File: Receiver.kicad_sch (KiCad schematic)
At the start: 20 parts, among them J2 UFL_Antennna, Y1 52Mhz/8pF, Y2 52Mhz/8pF

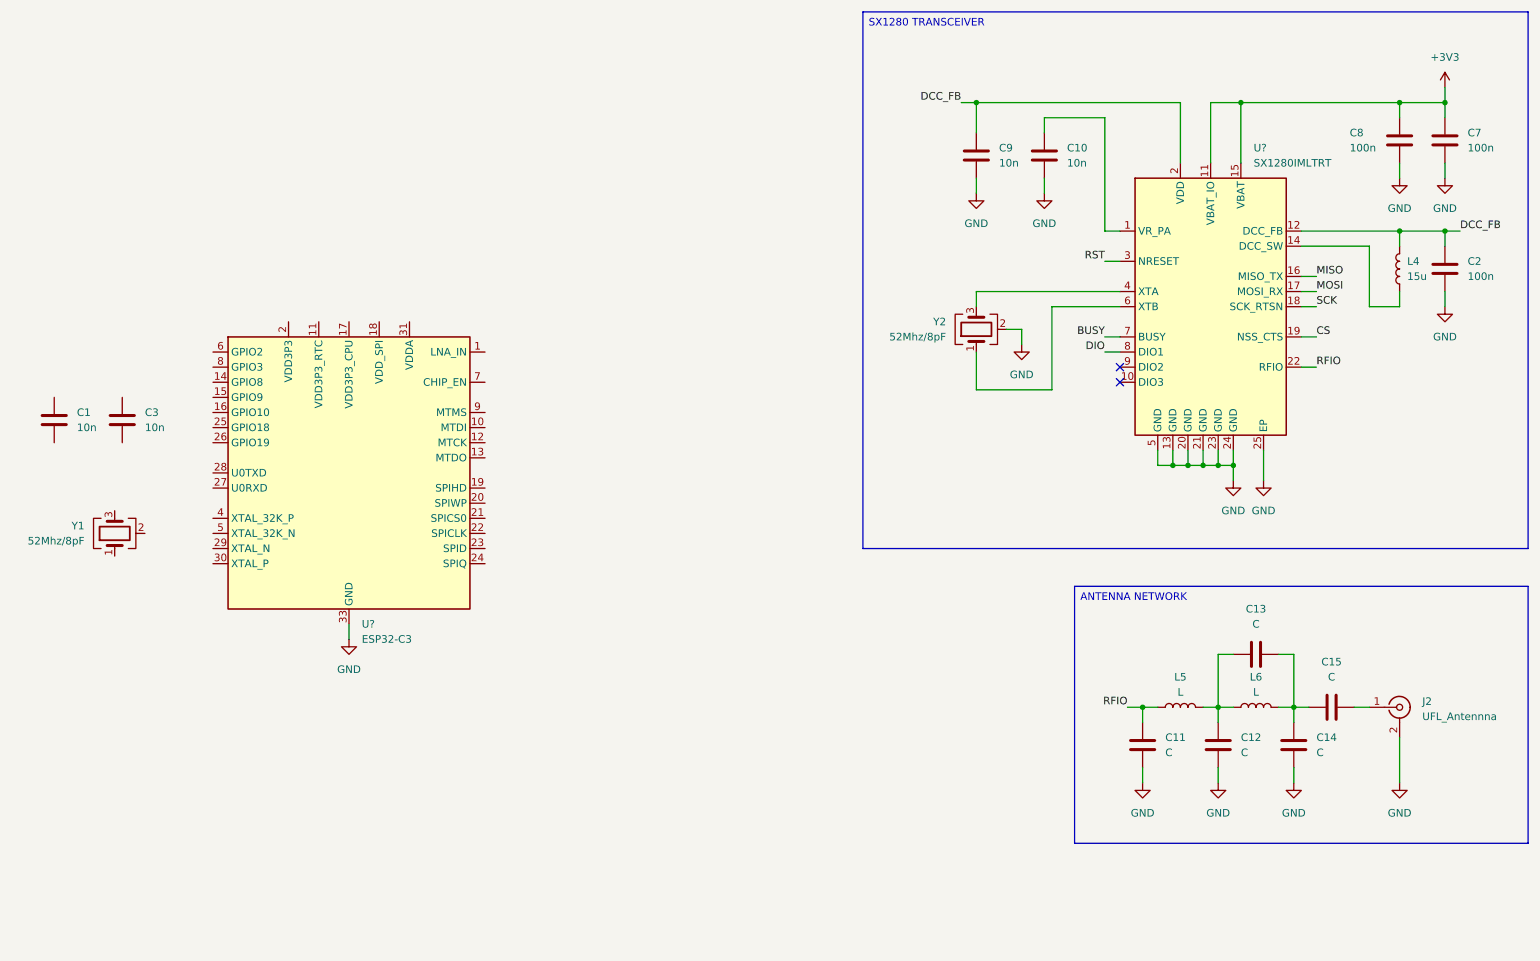
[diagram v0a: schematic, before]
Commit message: Receiver design
Updated the receiver schematic.

TODO:
Review the receiver schematic.
Implement sensor conditioning.
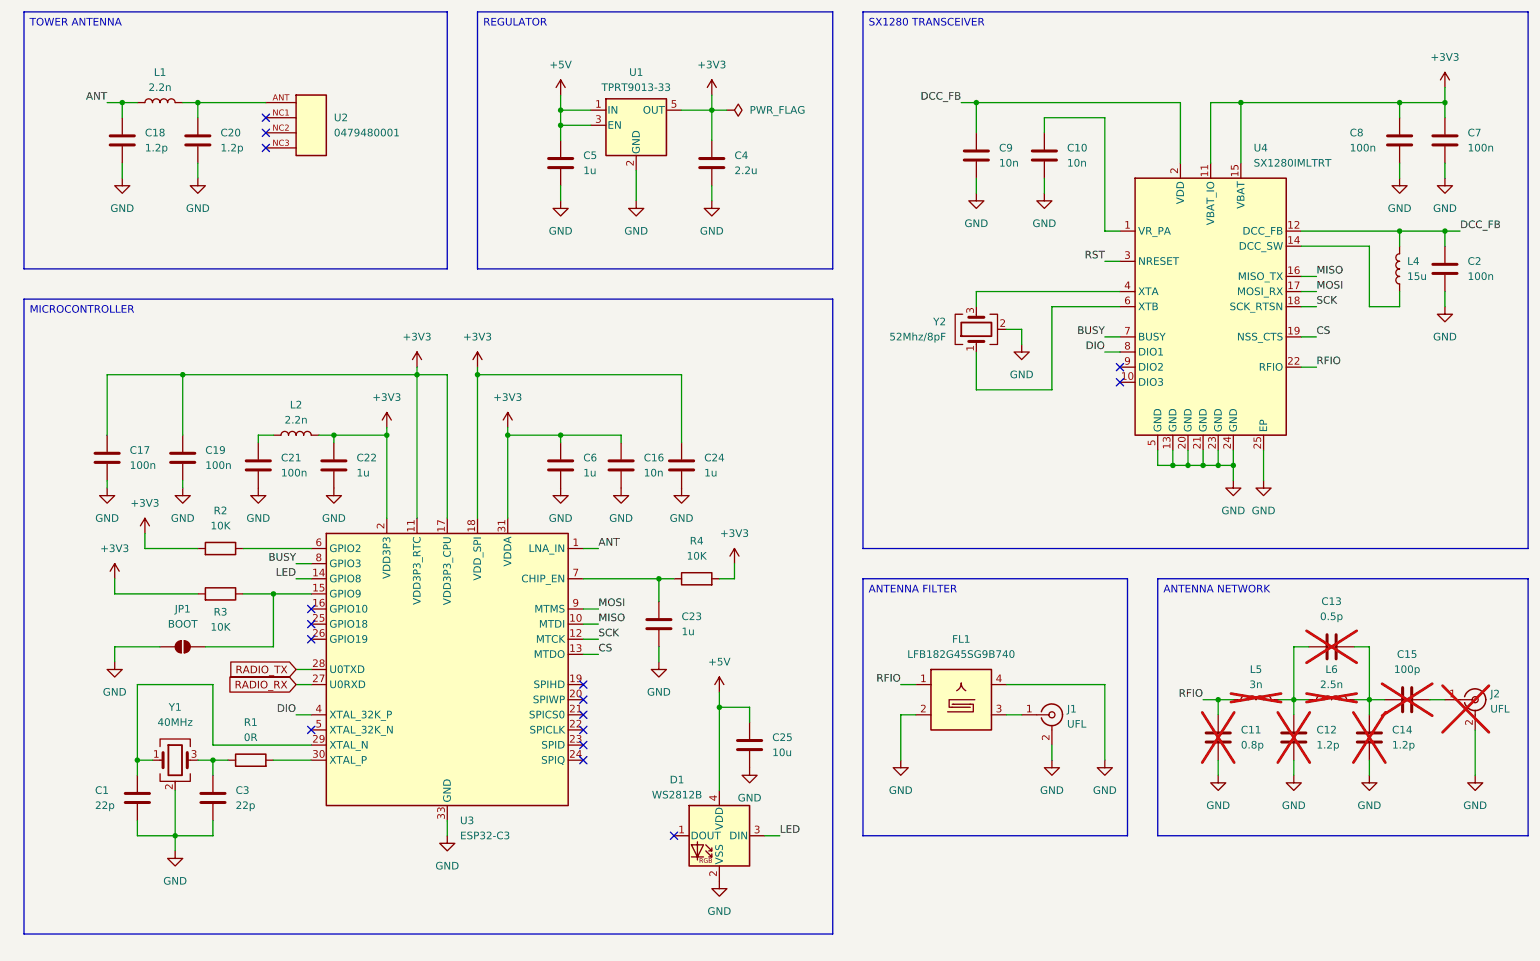
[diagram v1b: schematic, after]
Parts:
- added C16: 10n, symbol Device:C
- added C17, C19, C21: 100n, symbol Device:C
- added C18, C20: 1.2p, symbol Device:C
- added C22, C23, C24, C5, C6: 1u, symbol Device:C
- added C25: 10u, symbol Device:C
- added C4: 2.2u, symbol Device:C
- added D1: WS2812B, Custom_Parts:WS2812B-2020, symbol LED:WS2812B-2020
- added FL1: LFB182G45SG9B740, Custom_Parts:LFB182G45SG9B740, symbol Custom_Parts:LFB182G45SG9B740
- added J1: UFL, Connector_Coaxial:U.FL_Hirose_U.FL-R-SMT-1_Vertical, symbol Connector:Conn_Coaxial
- added JP1: BOOT, Jumper:SolderJumper-2_P1.3mm_Open_RoundedPad1.0x1.5mm, symbol Jumper:SolderJumper_2_Open
- added L1, L2: 2.2n, symbol Device:L
- added R1: 0R, symbol Device:R
- added R2, R3, R4: 10K, symbol Device:R
- added U1: TPRT9013-33, Package_TO_SOT_SMD:SOT-23-5, symbol Regulator_Linear:TLV70233_SOT23-5
- added U2: 0479480001, Custom_Parts:0479480001, symbol Custom_Parts:0479480001
- C1, C3: value 10n -> 22p
- C11: value C -> 0.8p; now not fitted; now left out of the parts list
- C12, C14: value C -> 1.2p; now not fitted; now left out of the parts list
- C13: value C -> 0.5p; now not fitted; now left out of the parts list
- C15: value C -> 100p; now not fitted; now left out of the parts list
- J2: value UFL_Antennna -> UFL; now not fitted; now left out of the parts list
- L5: value L -> 3n; now not fitted; now left out of the parts list
- L6: value L -> 2.5n; now not fitted; now left out of the parts list
- Y1: value 52Mhz/8pF -> 40MHz
- gave numbers to parts that had none: 2
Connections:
- net +3V3: now also U3.11 (VDD3P3_RTC), U3.17 (VDD3P3_CPU), U3.18 (VDD_SPI), U3.2 (VDD3P3), U3.3 (VDD3P3), U3.31 (VDDA), U3.32 (VDDA), C16.1, C17.1, C19.1, C22.1, C24.1, C4.1, C6.1, L2.2, R2.2, R3.2, R4.2, U1.5 (OUT)
- net BUSY: now also U3.8 (GPIO3)
- net CS: now also U3.13 (MTDO)
- net DIO: now also U3.4 (XTAL_32K_P)
- net GND: now also C1.2, C3.2, Y1.2 (G), Y1.4 (G), C16.2, C17.2, C18.2, C19.2, C20.2, C21.2, C22.2, C23.2, C24.2, C25.2, C4.2, C5.2, C6.2, D1.2 (VSS), FL1.2, FL1.4, FL1.5, J1.2 (Ext), JP1.1 (A), U1.2 (GND)
- net MISO: now also U3.10 (MTDI)
- net MOSI: now also U3.9 (MTMS)
- net RFIO: now also FL1.1
- net SCK: now also U3.12 (MTCK)
- net ANT: now reaches U3.1 (LNA_IN)
- net ANT: now also C18.1, L1.1
- net LED: now reaches U3.14 (GPIO8)
- net LED: now also D1.3 (DIN)
- net at U3.15 (GPIO9): now also JP1.2 (B), R3.1
- net RADIO_RX: now reaches U3.27 (U0RXD)
- net RADIO_TX: now reaches U3.28 (U0TXD)
- net at U3.29 (XTAL_N): now also C1.1, Y1.1
- net at U3.30 (XTAL_P): now also R1.2
- net at U3.6 (GPIO2): now also R2.1
- net at U3.7 (CHIP_EN): now also C23.1, R4.1
- net at Y1.3: now also C3.1, R1.1
- new net: C20.1, L1.2, U2.ANT
- new net: C21.1, L2.1
- new net: FL1.3, J1.1 (In)
- new net +5V: C25.1, C5.1, D1.4 (VDD), U1.1 (IN), U1.3 (EN)
- no-connect marks 2 -> 16
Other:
- moved on the sheet: C1, C3, U3, Y1

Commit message: Sensors design
Updated the inertial measurement unit schematic.
Updated the power monitor schematic.
Updated the barometer schematic.
Updated the receiver schematic.

TODO:
Review the sensors schematic.
Implement ESC schematic.
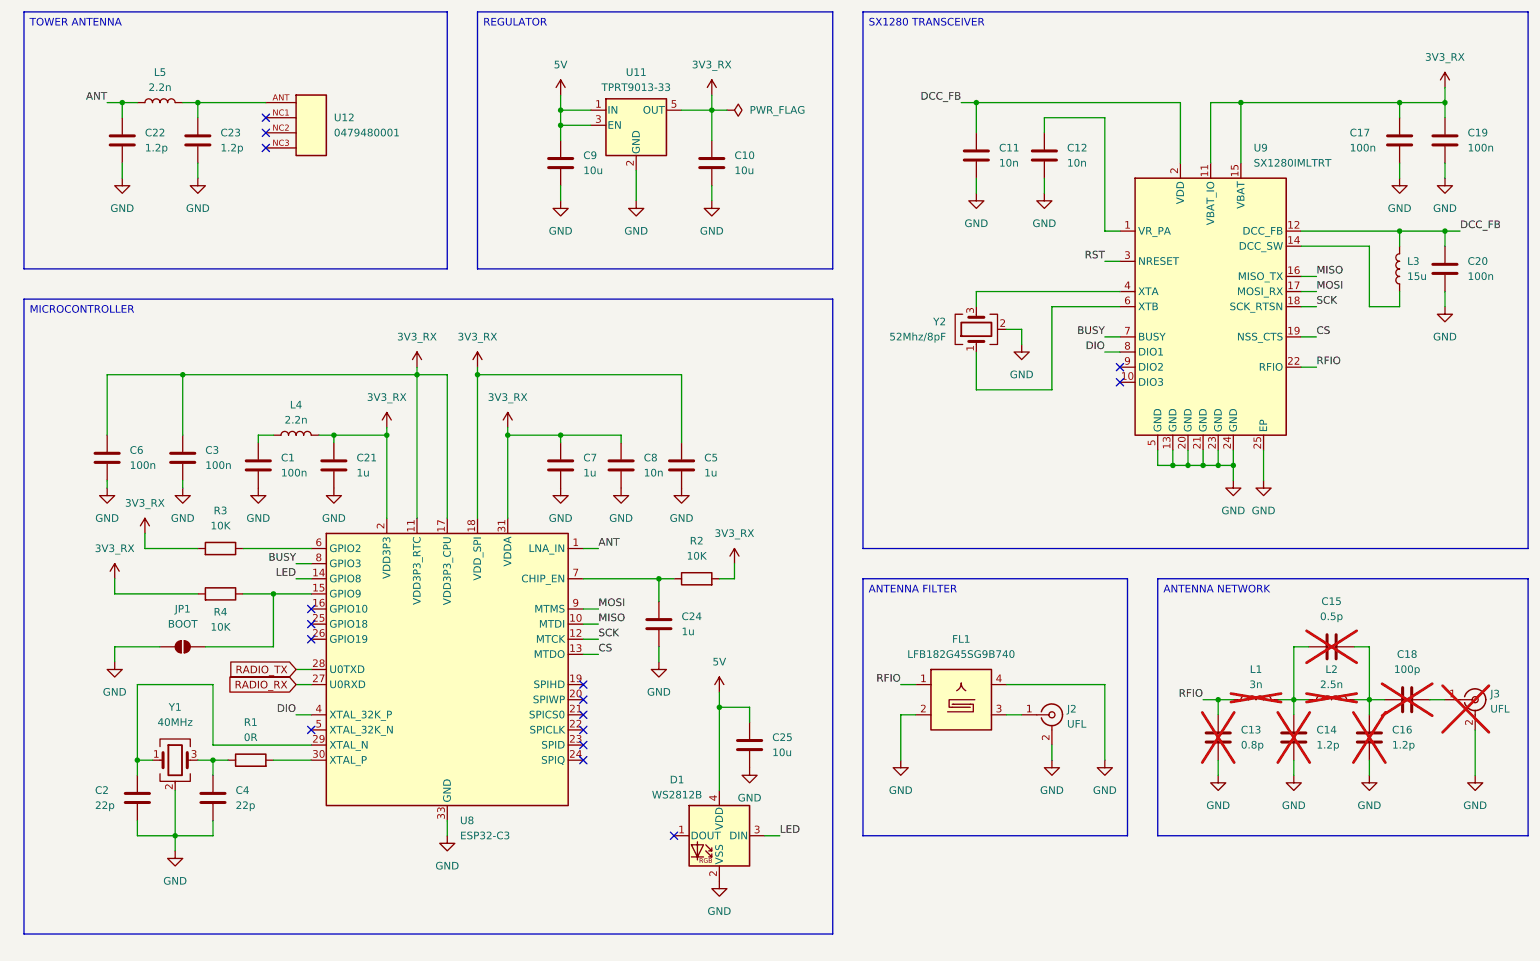
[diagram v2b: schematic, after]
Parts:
- C10: renamed from C4; value 2.2u -> 10u
- C9: renamed from C5; value 1u -> 10u
- renumbered C21 to C1, C9 to C11, C10 to C12, C11 to C13, C12 to C14, C13 to C15, C14 to C16, C8 to C17, C15 to C18, C7 to C19, C1 to C2, C2 to C20, C22 to C21, C18 to C22, C20 to C23, C23 to C24, C19 to C3, C3 to C4, C24 to C5, C17 to C6, C6 to C7, C16 to C8, J1 to J2, J2 to J3, L5 to L1, L6 to L2, L4 to L3, L2 to L4, L1 to L5, R4 to R2, R2 to R3, R3 to R4, U1 to U11, U2 to U12, U3 to U8, U4 to U9
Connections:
- net +3V3 renamed 3V3_RX
- net +5V renamed 5V

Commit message: ESC design
Updated the ESC schematic.
Replaces the INA 226 with INA230.
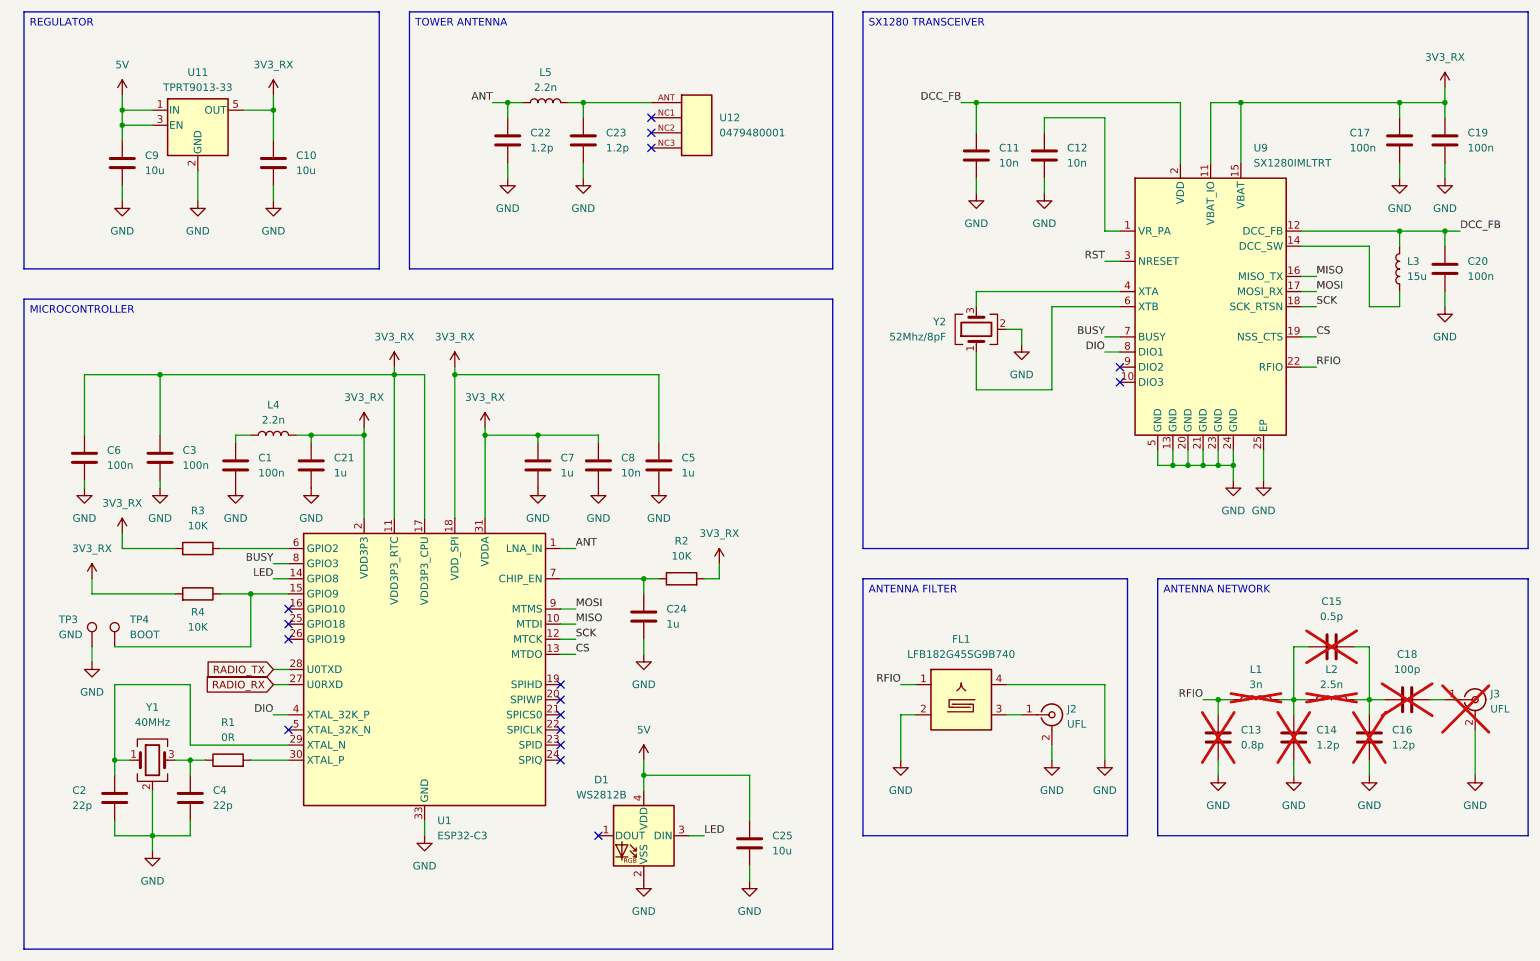
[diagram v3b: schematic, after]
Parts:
- removed JP1: BOOT, Jumper:SolderJumper-2_P1.3mm_Open_RoundedPad1.0x1.5mm, symbol Jumper:SolderJumper_2_Open
- removed U8: ESP32-C3, Package_DFN_QFN:QFN-32-1EP_5x5mm_P0.5mm_EP3.7x3.7mm, symbol MCU_Espressif:ESP32-C3
- added TP3: GND, TestPoint:TestPoint_Pad_D1.0mm, symbol Connector:TestPoint
- added TP4: BOOT, TestPoint:TestPoint_Pad_D1.0mm, symbol Connector:TestPoint
- added U1: ESP32-C3, Package_DFN_QFN:QFN-32-1EP_5x5mm_P0.5mm_EP3.7x3.7mm, symbol Custom_Parts:ESP32-C3
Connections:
- net 3V3_RX: now also U1.11 (VDD3P3_RTC), U1.17 (VDD3P3_CPU), U1.18 (VDD_SPI), U1.2 (VDD3P3), U1.3 (VDD3P3), U1.31 (VDDA), U1.32 (VDDA)
- net ANT: now also U1.1 (LNA_IN)
- net BUSY: now also U1.8 (GPIO3)
- net CS: now also U1.13 (MTDO)
- net DIO: now also U1.4 (XTAL_32K_P)
- net GND: now also TP3.1, U1.33 (GND)
- net LED: now also U1.14 (GPIO8)
- net MISO: now also U1.10 (MTDI)
- net MOSI: now also U1.9 (MTMS)
- net RADIO_RX: now also U1.27 (U0RXD)
- net RADIO_TX: now also U1.28 (U0TXD)
- net SCK: now also U1.12 (MTCK)
- net at R1.2: now also U1.30 (XTAL_P)
- net at R4.1: now also TP4.1, U1.15 (GPIO9)
- net at C2.1, Y1.1: now also U1.29 (XTAL_N)
- net at R3.1: now also U1.6 (GPIO2)
- net at C24.1, R2.1: now also U1.7 (CHIP_EN)
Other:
- moved on the sheet: C1, C10, C2, C21, C22, C23, C24, C25, C3, C4, C5, C6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

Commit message: MCU design
Updated the main RP2350 schematic.
Updated labels for other designs.
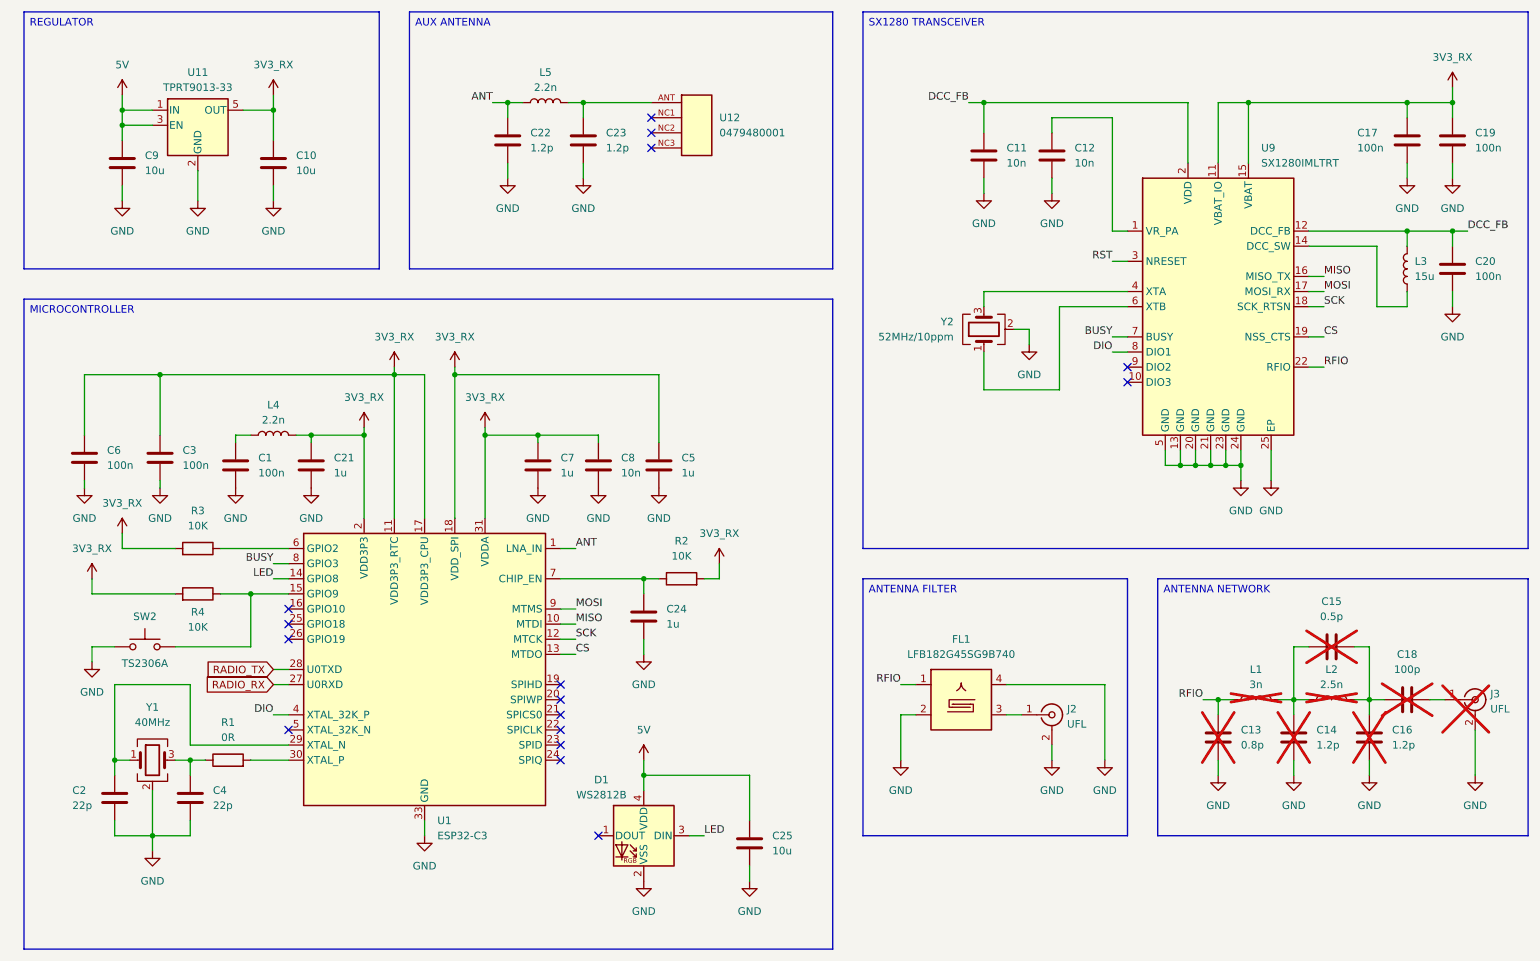
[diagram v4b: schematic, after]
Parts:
- removed TP3: GND, TestPoint:TestPoint_Pad_D1.0mm, symbol Connector:TestPoint
- removed TP4: BOOT, TestPoint:TestPoint_Pad_D1.0mm, symbol Connector:TestPoint
- added SW2: TS2306A, Custom_Parts:SW_SMD_3.0x2.0_PUSH, symbol Switch:SW_Push
- Y2: value 52Mhz/8pF -> 52MHz/10ppm
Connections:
- net GND: now also SW2.1
- net at R4.1, U1.15 (GPIO9): now also SW2.2
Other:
- moved on the sheet: C11, C12, C17, C19, C20, L3, U9, Y2
